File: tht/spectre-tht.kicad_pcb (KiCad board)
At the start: 2 copper layers, 46 x 40 mm, 38 parts, among them J1 12V IN, J2 LED 12V, J3 HALL, J4 LDR, Q1 2N2222A, Q2 2N2222A, Q3 2N2222A, Q4 IRLZ44N, U1 LM7805, U3 LM393

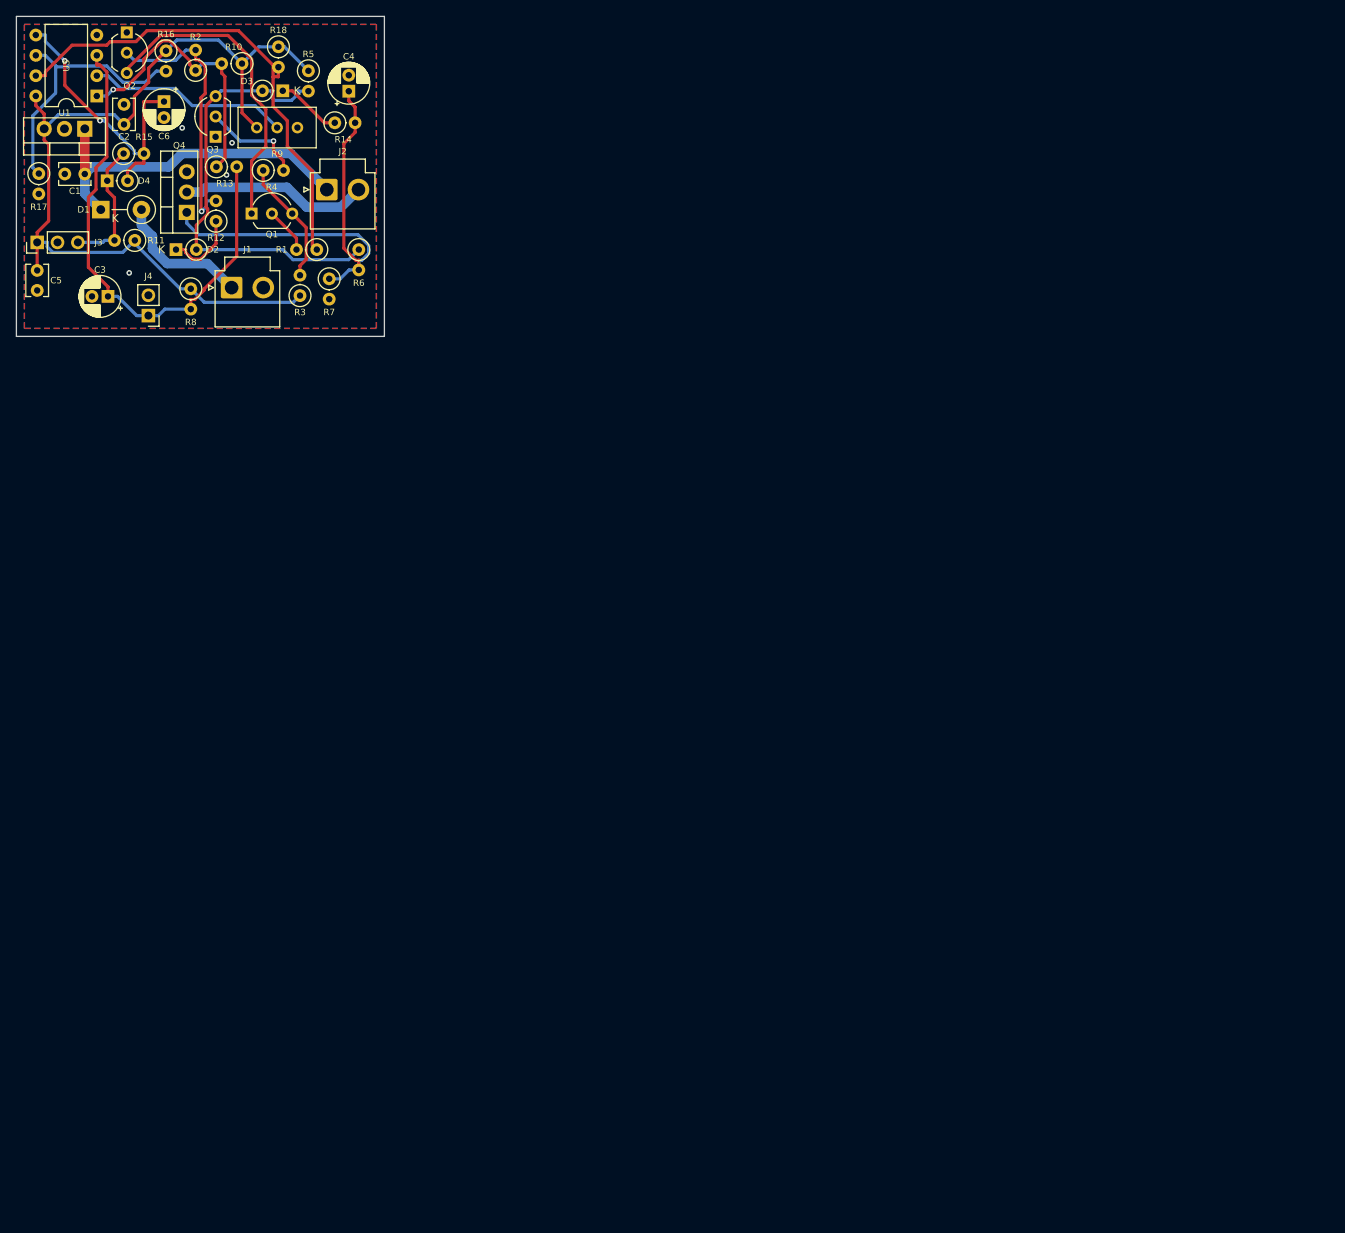
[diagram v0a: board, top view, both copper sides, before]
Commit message: THT rev E: apagado automático con CD4541, fade simétrico y menor consumo
- Esquemático propio de la versión THT (KiCad 7) y PCB de 64 x 50 mm.
- U4 CD4541 apaga la tira ~10 min después de abrir; se reinicia al cerrar.
- Fade con caminos separados de encendido (D3+R14) y apagado (D5+R6).
- LP2950-5.0 y Q3 PNP: consumo en reposo de ~14 mA a ~5 mA.
- DRC sin errores; netlist esquemático vs PCB sin diferencias.
- Se retiran los Gerbers de rev D (siguen en la etiqueta tht-rev-d).

Co-Authored-By: Claude Opus 5.5 <noreply@anthropic.com>
Claude-Session: https://claude.ai/code/session_018mBD4zSdnh6yTbdGDUV7b8
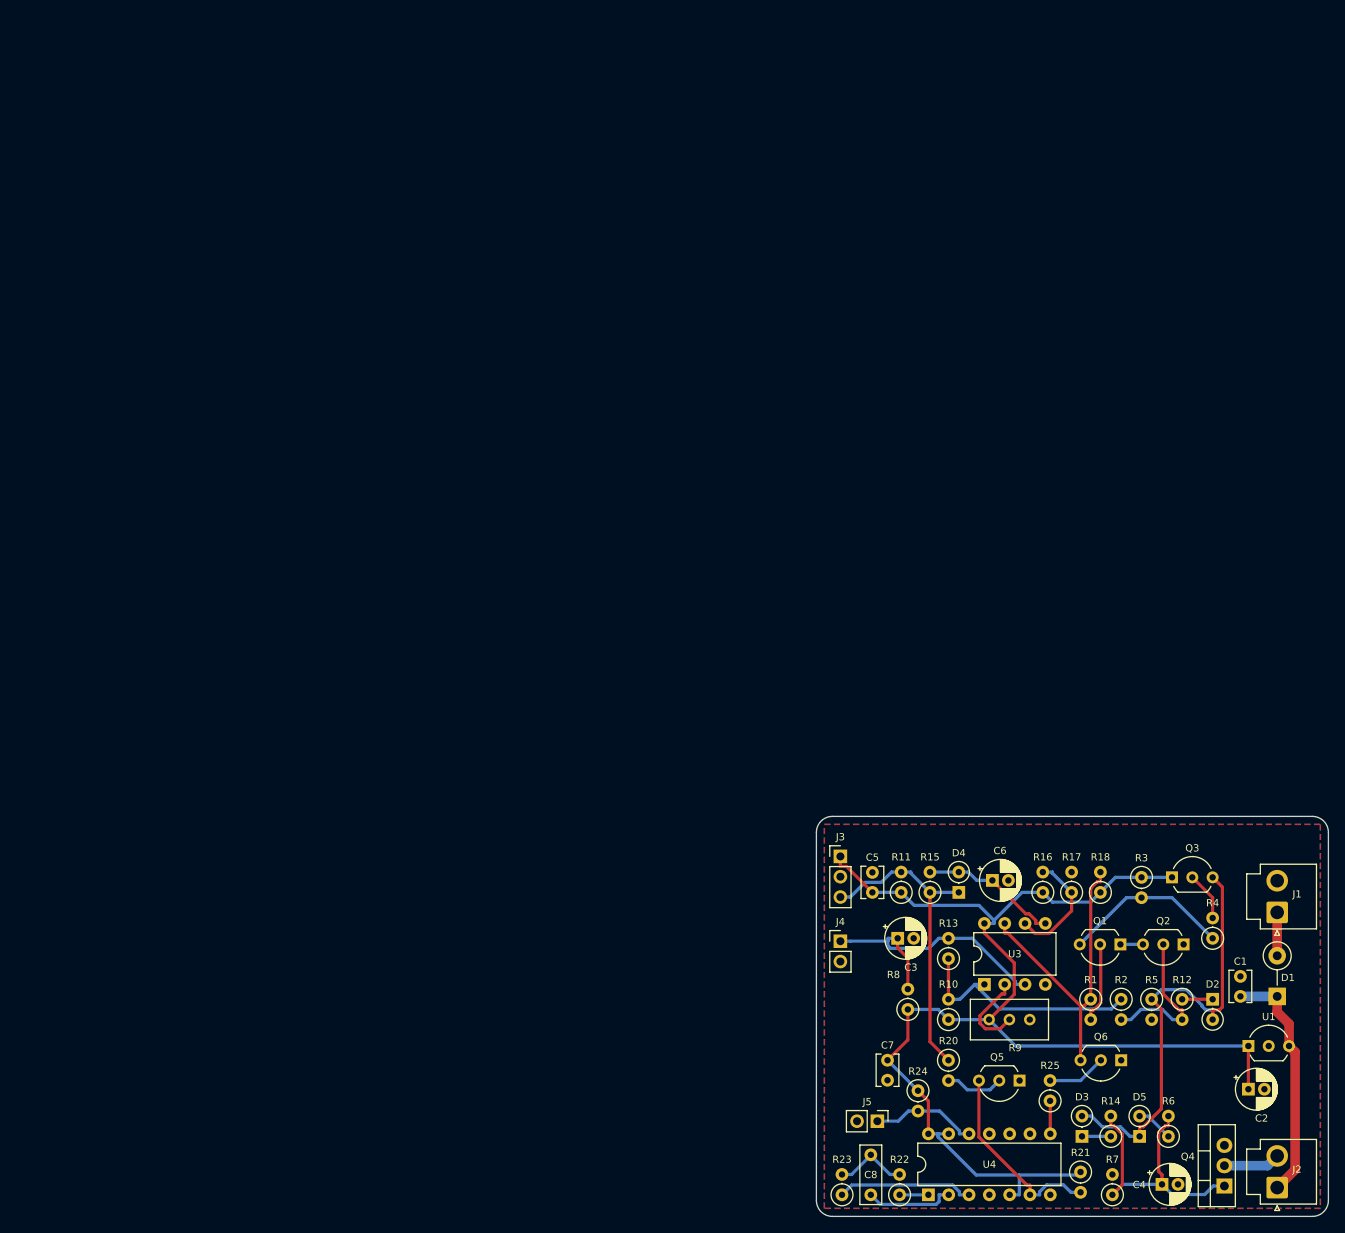
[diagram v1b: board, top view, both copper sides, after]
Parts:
- added C7: 0.1uF, Capacitor_THT:C_Disc_D3.8mm_W2.6mm_P2.50mm, F.Cu at (108.9, 130.5)
- added C8: 100nF film, Capacitor_THT:C_Rect_L7.2mm_W2.5mm_P5.00mm_FKS2_FKP2_MKS2_MKP2, F.Cu at (106.8, 147.3)
- added D5: 1N4148, Diode_THT:D_DO-35_SOD27_P2.54mm_Vertical_KathodeUp, F.Cu at (140.4, 140.0)
- added J5: TEST, Connector_PinHeader_2.54mm:PinHeader_1x02_P2.54mm_Vertical, F.Cu at (107.6, 138.1)
- added Q5: PN2222A, Package_TO_SOT_THT:TO-92_Inline_Wide, F.Cu at (125.4, 133.0)
- added Q6: PN2222A, Package_TO_SOT_THT:TO-92_Inline_Wide, F.Cu at (138.1, 130.5)
- added R20: 220k, Resistor_THT:R_Axial_DIN0207_L6.3mm_D2.5mm_P2.54mm_Vertical, F.Cu at (116.5, 130.5)
- added R21: 100k, Resistor_THT:R_Axial_DIN0207_L6.3mm_D2.5mm_P2.54mm_Vertical, F.Cu at (133.0, 144.4)
- added R22: 82k, Resistor_THT:R_Axial_DIN0207_L6.3mm_D2.5mm_P2.54mm_Vertical, F.Cu at (110.4, 147.3)
- added R23: 180k, Resistor_THT:R_Axial_DIN0207_L6.3mm_D2.5mm_P2.54mm_Vertical, F.Cu at (103.2, 147.3)
- added R24: 100k, Resistor_THT:R_Axial_DIN0207_L6.3mm_D2.5mm_P2.54mm_Vertical, F.Cu at (112.7, 134.3)
- added R25: 10k, Resistor_THT:R_Axial_DIN0207_L6.3mm_D2.5mm_P2.54mm_Vertical, F.Cu at (129.2, 135.6)
- added U4: CD4541BE, Package_DIP:DIP-14_W7.62mm, F.Cu at (114.0, 147.3)
- C2: value 0.1uF -> 10uF 16V; footprint Capacitor_THT:C_Disc_D3.8mm_W2.6mm_P2.50mm -> Capacitor_THT:CP_Radial_D5.0mm_P2.00mm
- Q1, Q2: value 2N2222A -> PN2222A
- Q3: value 2N2222A -> 2N3906
- R5: value 1k -> 4.7k
- R6: value 100k -> 39k
- R9: value 10k 3296W -> 10k trim
- U1: value LM7805 -> LP2950-5.0; footprint Package_TO_SOT_THT:TO-220-3_Vertical -> Package_TO_SOT_THT:TO-92_Inline_Wide
- moved U1 185.2 mm to (154.0, 128.7), turned to 0 degrees
- moved C2 185.2 mm to (154.0, 134.1), turned to 0 degrees
- moved Q4 177.9 mm to (151.0, 146.2)
- moved C1 177.3 mm to (153.0, 122.5), turned to 90 degrees
- moved D1 176.9 mm to (157.6, 122.5), turned to 90 degrees
- moved Q2 174.5 mm to (145.9, 116.0), turned to 180 degrees
- moved J2 172.3 mm to (157.6, 146.4), turned to 90 degrees
- moved C4 170.3 mm to (143.2, 146.0), turned to 0 degrees
- moved D3 164.5 mm to (133.2, 140.0), turned to 90 degrees
- moved R2 163.9 mm to (138.1, 122.9), turned to -90 degrees
- moved D2 159.9 mm to (149.5, 122.9), turned to -90 degrees
- moved R14 159.6 mm to (136.8, 140.0), turned to 90 degrees
- moved R17 157.3 mm to (131.9, 109.5), turned to 90 degrees
- moved U3 157.0 mm to (121.0, 121.0), turned to 90 degrees
- moved R5 156.8 mm to (141.9, 122.9)
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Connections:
- net Net-(Q1-B) renamed /Q1_B
- net Net-(Q1-E) renamed /Q1_E
- net Net-(Q2-B) renamed /Q2_B
- net Net-(Q3-B) renamed /Q3_B
- Q3 pad 1: GND -> +5V
- R5 pad 1: +5V -> /NODO_B
- R5 pad 2: /NODO_B -> GND
- R6 pad 1: /NODO_B -> /SLOW
- U1 pad 1: +12V -> +5V
- U1 pad 3: +5V -> +12V
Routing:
- net +5V: track 114.1 -> 160.3 mm
- net /Q1_E: track 39.8 -> 2.82 mm
- net /LDR_DIV: track 65.0 -> 35.4 mm
- net /MR: track 0.00 -> 24.6 mm
- net /HALL_OUT: track 16.8 -> 39.2 mm
- net /ARM: track 61.2 -> 39.5 mm
- net /GATE: track 57.4 -> 36.1 mm
- net /VTH: track 33.3 -> 14.6 mm
- net /DELAY: track 36.0 -> 17.3 mm, vias 2 -> 0
- net /RS: track 0.00 -> 17.1 mm
- net /LED_NEG: track 23.6 -> 7.11 mm
- net /REF: track 25.2 -> 10.8 mm
- net /Q2_B: track 33.4 -> 19.3 mm, vias 1 -> 0
- net +12V: track 44.1 -> 30.3 mm
- net /TSEL: track 0.00 -> 13.4 mm
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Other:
- board size 46 x 40 mm -> 64 x 50 mm

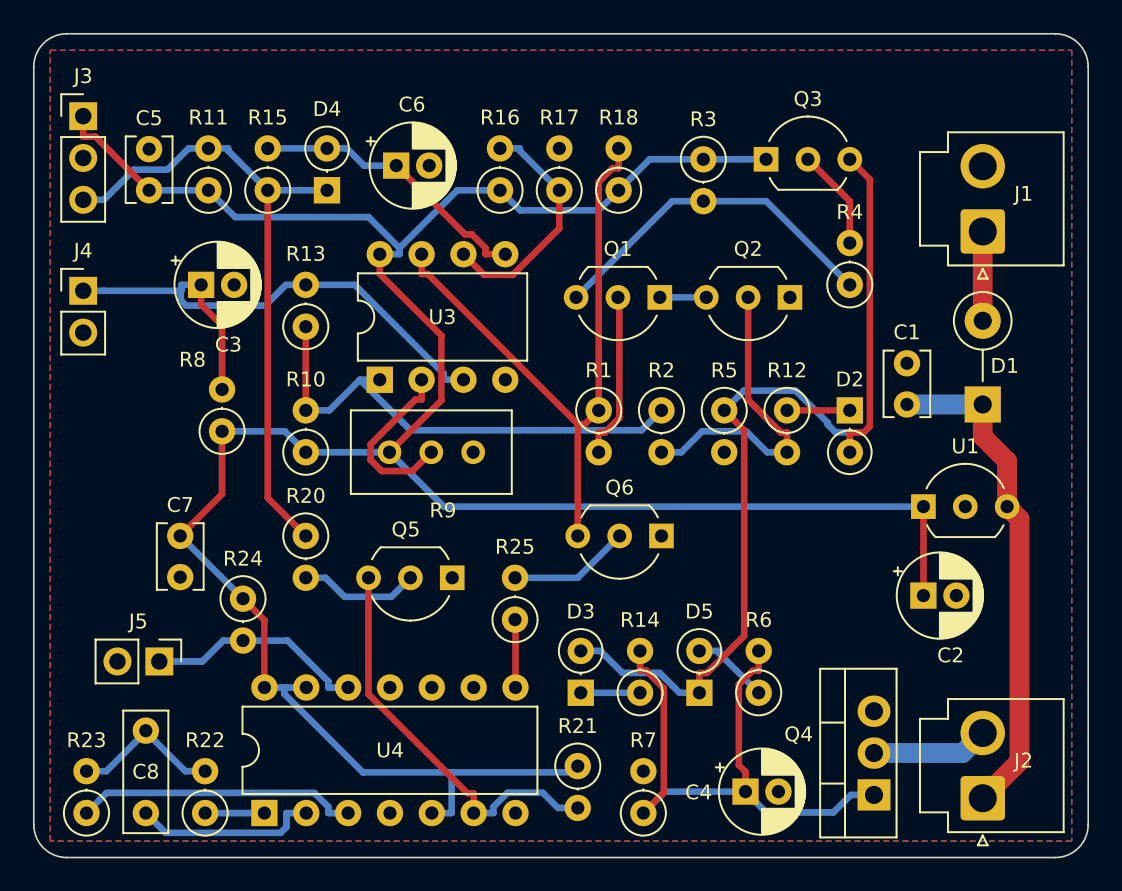
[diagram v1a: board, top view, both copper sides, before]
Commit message: THT rev E: acomodo redistribuido y Gerbers regenerados
- Conectores con el mismo margen al borde (~1.1 mm).
- D1 y C1 horizontales; cátodo de D1, C1 y entrada de U1 en una vertical.
- Filas alineadas: J4/C3/R13 con U3, R8/C7/R10 con R9,
  J5/R24/R20/Q5/R25/Q6 con espacio repartido; U4 y oscilador 1.5 mm arriba.
- Mismo circuito y misma netlist; ruteo nuevo sin vías y DRC sin errores.

Co-Authored-By: Claude Opus 5.5 <noreply@anthropic.com>
Claude-Session: https://claude.ai/code/session_018mBD4zSdnh6yTbdGDUV7b8
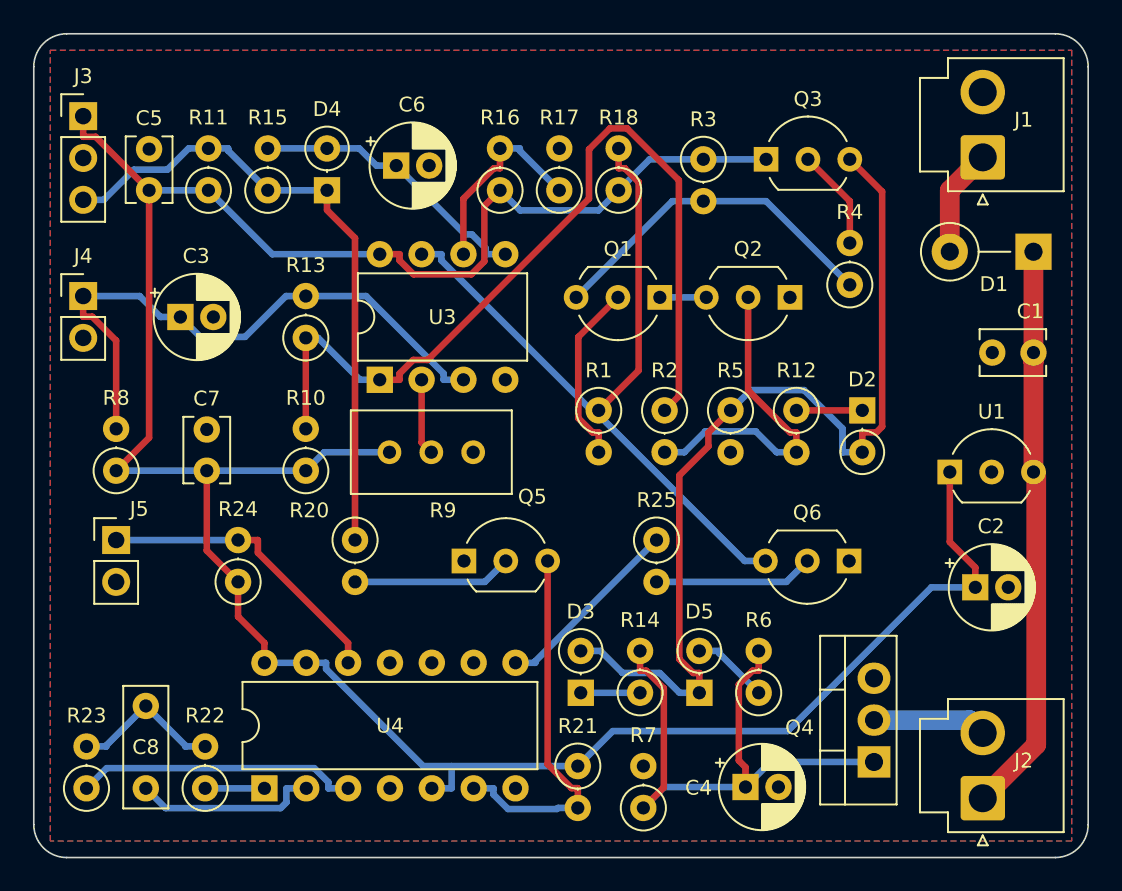
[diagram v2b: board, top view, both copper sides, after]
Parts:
- moved Q6 11.5 mm to (149.5, 132.0)
- moved R25 9.85 mm to (137.8, 130.7), turned to -90 degrees
- moved D1 9.77 mm to (160.7, 113.2), turned to 180 degrees
- moved C1 8.30 mm to (160.7, 119.3), turned to 180 degrees
- moved J5 7.82 mm to (105.0, 130.7), turned to 0 degrees
- moved R8 6.86 mm to (105.0, 126.5)
- moved J1 4.50 mm to (157.6, 107.5)
- moved C7 4.27 mm to (110.5, 126.5), turned to 90 degrees
- moved C2 3.19 mm to (157.2, 133.6)
- moved R20 3.00 mm to (119.5, 130.7)
- moved U1 2.64 mm to (155.6, 126.6)
- moved C3 2.32 mm to (108.9, 117.2)
- moved Q4 2.00 mm to (151.0, 144.2)
- moved C8 1.50 mm to (106.8, 145.8)
- moved R22 1.50 mm to (110.4, 145.8)
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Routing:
- net /CMP_OUT: track 30.4 -> 53.1 mm
- net /TOUT: track 4.13 -> 11.7 mm
- net /ARM: track 39.5 -> 46.6 mm
- net /REF: track 10.8 -> 4.64 mm
- net /TSEL: track 13.4 -> 18.3 mm
- net +12V: track 30.3 -> 35.2 mm
- net /Q5_B: track 7.31 -> 9.68 mm
- net /Q6_B: track 7.40 -> 9.68 mm
- net /VTH: track 14.6 -> 12.3 mm
- net /MR: track 24.6 -> 23.1 mm
- net /LDR_DIV: track 35.4 -> 36.7 mm
- net /+12V_IN: track 5.42 -> 6.56 mm
- net /Q1_B: track 10.2 -> 11.1 mm
- net /GATE: track 36.1 -> 35.2 mm
- net /NODO_B: track 57.0 -> 57.9 mm
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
